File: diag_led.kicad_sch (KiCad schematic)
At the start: 3 parts, among them Q1301 BSS84

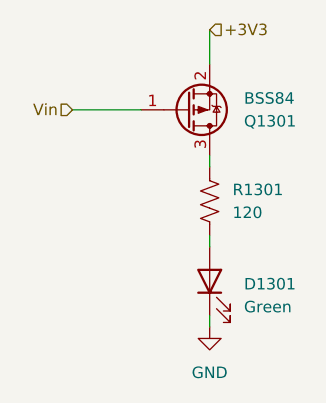
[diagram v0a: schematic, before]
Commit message: quicksave on some R.S. T.S. (mostly layout changes, small pin changes for better routing)
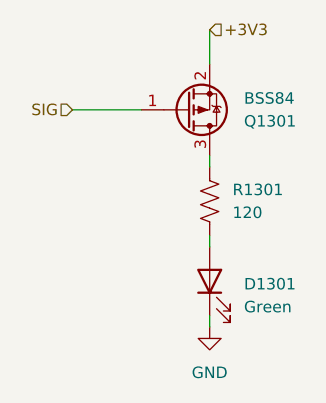
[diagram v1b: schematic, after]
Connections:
- net Vin renamed SIG
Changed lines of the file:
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@@
 		)
 	)
-	(hierarchical_label "Vin"
+	(hierarchical_label "SIG"
 		(shape input)
 		(at 125.73 83.82 180)
